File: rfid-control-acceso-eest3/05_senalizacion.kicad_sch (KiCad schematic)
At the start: 9 parts, among them Q1 AO3400A_PRELIM

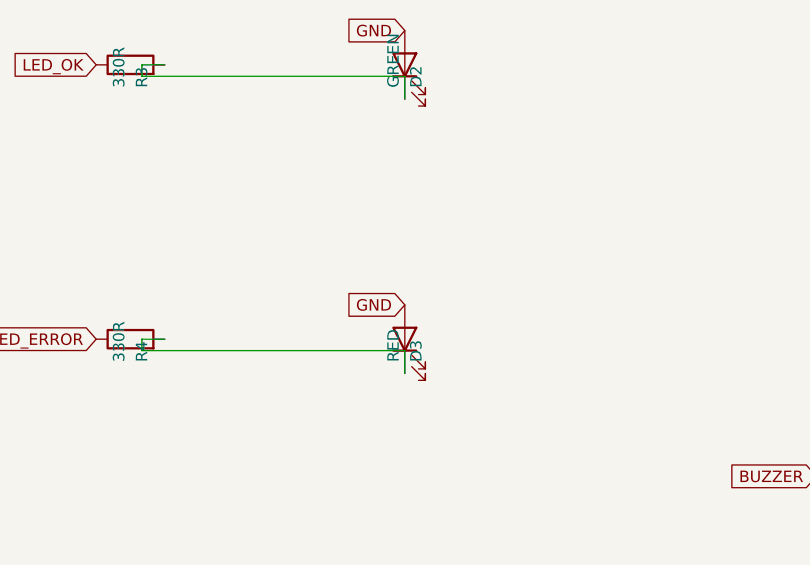
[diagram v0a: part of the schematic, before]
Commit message: Corrige tres diodos invertidos, netclasses y recalcula el floorplan
Errores electricos, verificados regenerando el netlist con kicad-cli:

- D1 tenia el catodo en +12V_IN y el anodo hacia F1, o sea bloqueaba la
  polaridad correcta. Montado asi la placa no encendia.
- D2 y D3 tenian el anodo a GND y el catodo hacia R3/R4. Como un GPIO nunca
  baja de 0 V, los LEDs no podian encender.
- La red entre D1 y F1 no coincidia con ningun patron de netclass y heredaba
  Default: 0,2 mm de pista para ~2,2 A. Pasa a LOCK_POWER (2,0 mm), igual que
  +12V_IN, que estaba en POWER_12V_AUX (0,8 mm).
- Al girar los LEDs, KiCad renombro las redes autogeneradas. Las netclasses
  apuntaban a los nombres viejos; se re-apuntaron.

Footprints: se eliminan los ocho PLACEHOLDER_NO_FABRICAR. Todos tenian
equivalente real ya instalado en KiCad 10. C9 pasa a MLCC 1206: tenia simbolo
no polarizado con footprint de electrolitico. El unico footprint local que
queda es el del ESP32-S3, con la hilera par duplicada en 22,86 y 25,40 mm
porque no se midio el modulo fisico. El paso doble cubre la separacion, no el
orden de pines: hay que verificar 3V3, EN, 5V y GND por continuidad antes de
soldar.

Floorplan: la posicion real de los pines de J13 determina el orden de los
bloques, y estaban casi invertidos. Lazo de potencia J1-J9 de 86 a 38 mm,
estrella de masa NT1-J1 de 60 a 9 mm, SPI de ~70 a 8,7 mm. Contorno de 120x80
a 140x100 mm: la densidad bajaba de 53% a 36% y la caja sigue sin definir.

Sigue sin ruteo, sin vias y sin archivos de fabricacion. Falta ejecutar
Update PCB from Schematic en la GUI: KiCad no expone esa operacion por CLI.

Co-Authored-By: Claude Opus 5 <noreply@anthropic.com>
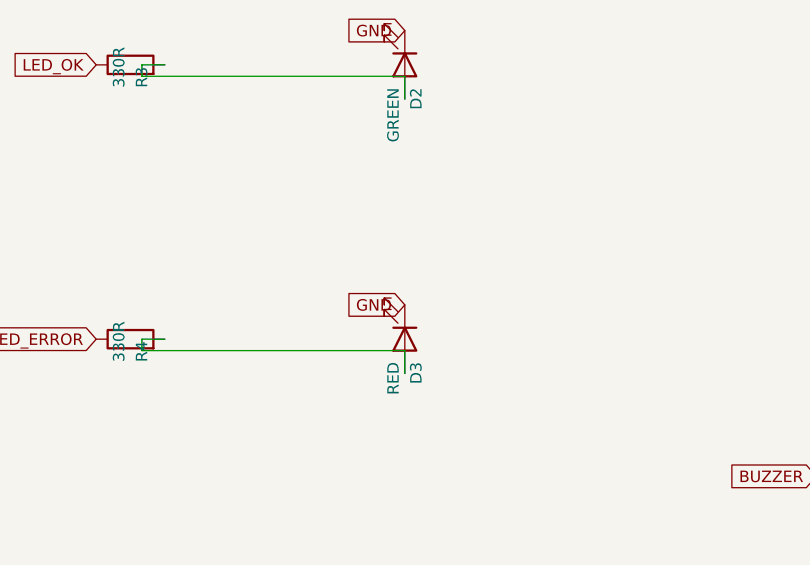
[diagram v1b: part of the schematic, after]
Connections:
- net GND: now also D2.1 (K), D3.1 (K); no longer D2.2 (A), D3.2 (A)
- net at R3.2: now also D2.2 (A); no longer D2.1 (K)
- net at R4.2: now also D3.2 (A); no longer D3.1 (K)
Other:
- moved on the sheet: D2, D3
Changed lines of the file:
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@@
 	(symbol
 		(lib_id "Device:LED")
-		(at 90.17 74.93 90)
+		(at 90.17 74.93 270)
 		(unit 1)
 		(body_style 1)
@@
 	(symbol
 		(lib_id "Device:LED")
-		(at 90.17 44.45 90)
-		(unit 1)
-		(body_style 1)
+		(at 90.17 44.45 270)
+		(unit 1)
+		(body_style 1)
